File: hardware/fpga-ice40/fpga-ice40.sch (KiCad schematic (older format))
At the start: 85 parts, among them J1 MicroSD_Molex_1040310811, J2 ProgHeader_iCE40, J3 ProgHeader_Flash_QSPI, J4 Conn_02x20_Odd_Even, U1 iCE40HX4K-TQ144, U2 IS42S16320F-6TL, U3 W25Q32JVSS, U4 W25Q32JVSS, U5 S25FL256SAGMFI01, U6 S25FL256SAGMFI01, U7 FT245RL

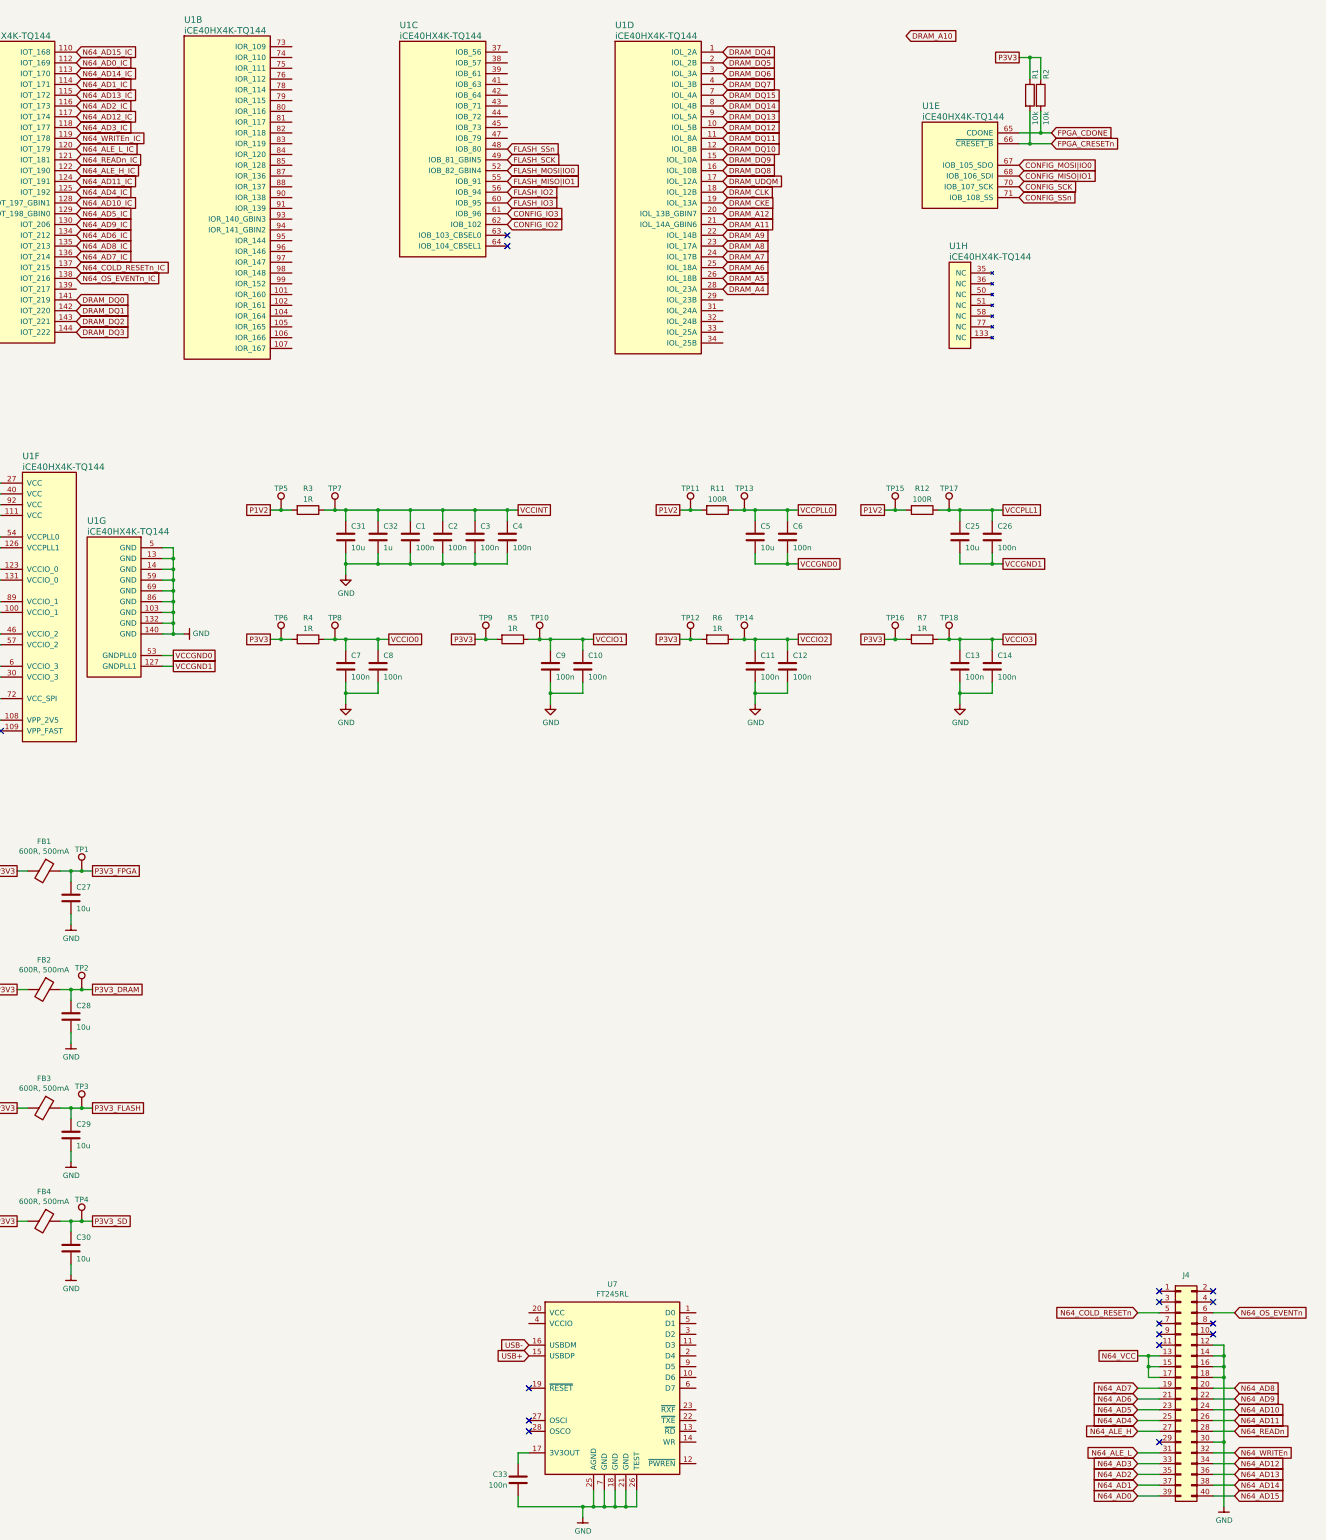
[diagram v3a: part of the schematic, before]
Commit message: Routing fpga to memory
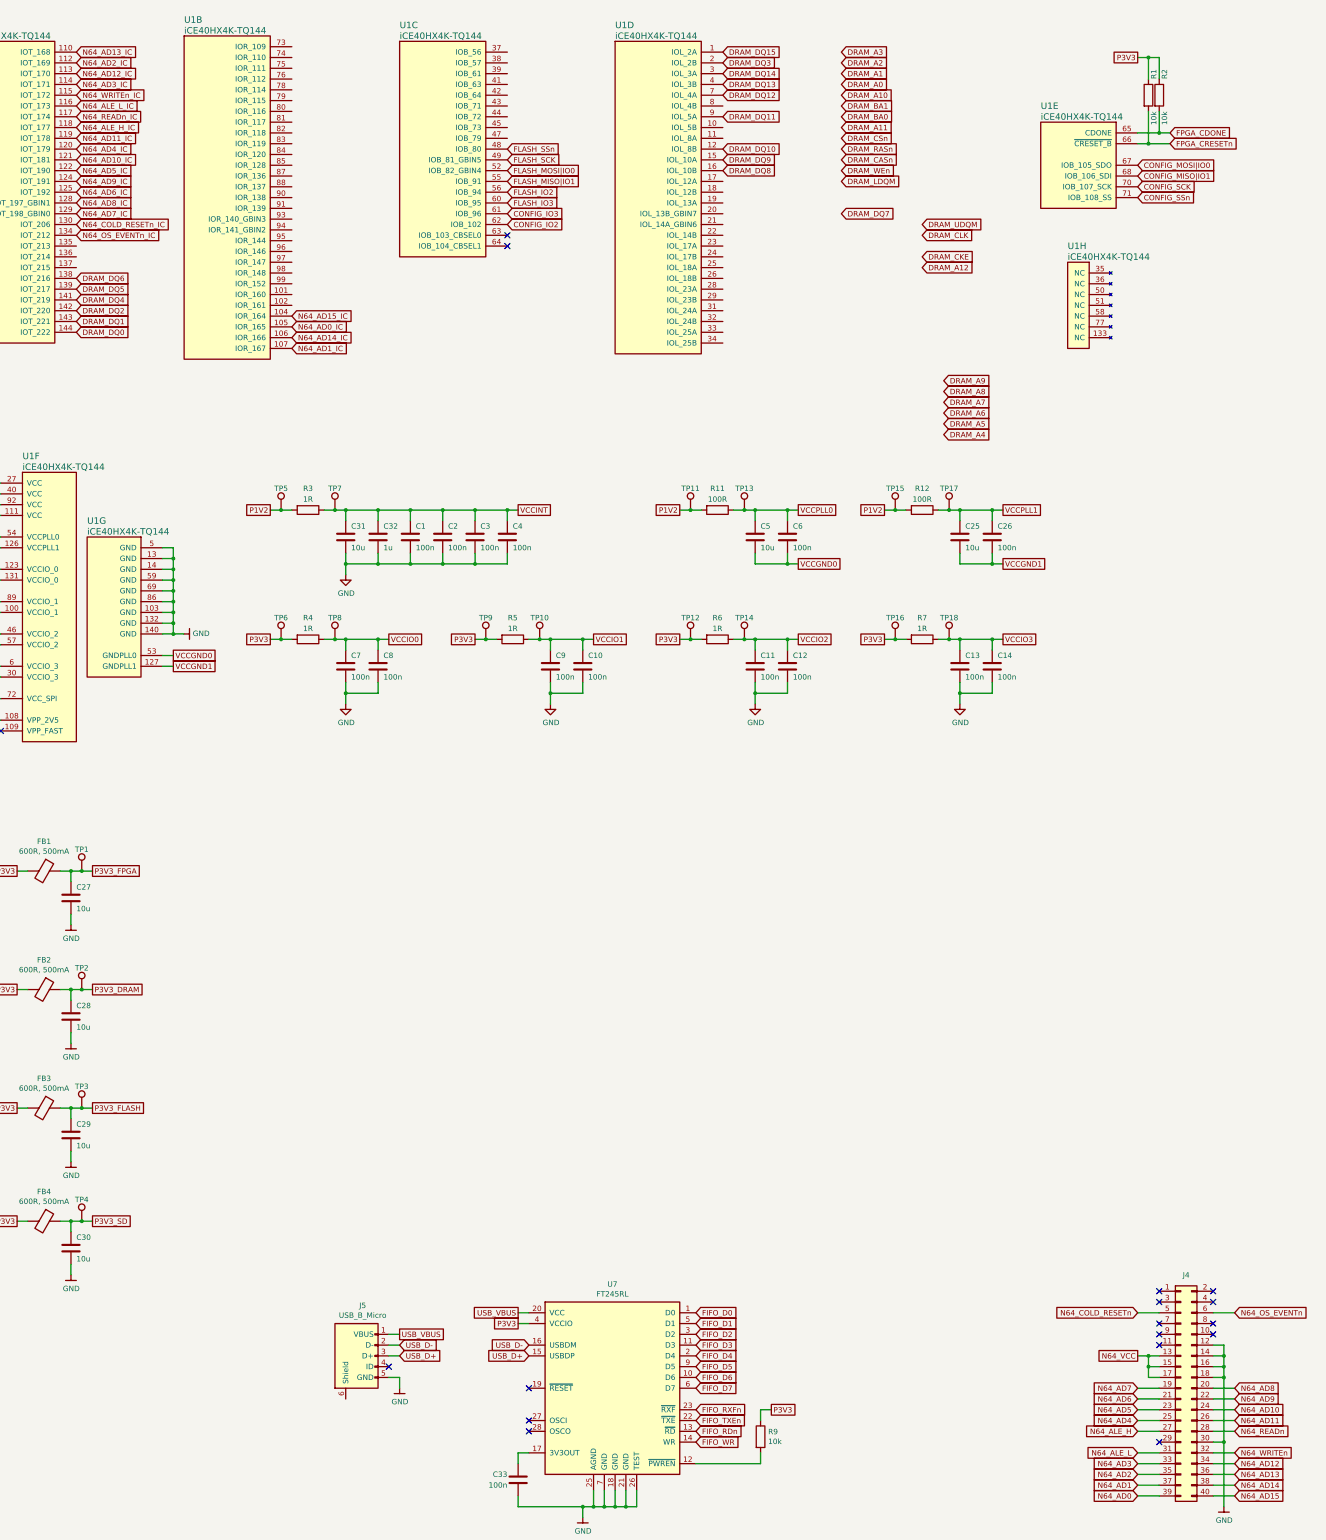
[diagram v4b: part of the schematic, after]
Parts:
- added J5: USB_B_Micro, Connector_USB:USB_Micro-B_Wuerth_629105150521, symbol ng_conn:USB_B_Micro
- added R9: 10k, Resistor_SMD:R_0603_1608Metric, symbol Device:R
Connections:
- net DRAM_A11: no longer U1.21 (IOL_14A_GBIN6)
- net DRAM_A12: no longer U1.20 (IOL_13B_GBIN7)
- net DRAM_A4: no longer U1.28 (IOL_23A)
- net DRAM_A5: no longer U1.26 (IOL_18B)
- net DRAM_A6: no longer U1.25 (IOL_18A)
- net DRAM_A7: no longer U1.24 (IOL_17B)
- net DRAM_A8: no longer U1.23 (IOL_17A)
- net DRAM_A9: no longer U1.22 (IOL_14B)
- net DRAM_CKE: no longer U1.19 (IOL_13A)
- net DRAM_CLK: no longer U1.18 (IOL_12B)
- net DRAM_DQ0: now also U1.144 (IOT_222); no longer U1.141 (IOT_219)
- net DRAM_DQ1: now also U1.143 (IOT_221); no longer U1.142 (IOT_220)
- net DRAM_DQ11: now also U1.9 (IOL_5A); no longer U1.11 (IOL_8A)
- net DRAM_DQ12: now also U1.7 (IOL_4A); no longer U1.10 (IOL_5B)
- net DRAM_DQ13: now also U1.4 (IOL_3B); no longer U1.9 (IOL_5A)
- net DRAM_DQ14: now also U1.3 (IOL_3A); no longer U1.8 (IOL_4B)
- net DRAM_DQ15: now also U1.1 (IOL_2A); no longer U1.7 (IOL_4A)
- net DRAM_DQ2: now also U1.142 (IOT_220); no longer U1.143 (IOT_221)
- net DRAM_DQ3: now also U1.2 (IOL_2B); no longer U1.144 (IOT_222)
- net DRAM_DQ4: now also U1.141 (IOT_219); no longer U1.1 (IOL_2A)
- net DRAM_DQ5: now also U1.139 (IOT_217); no longer U1.2 (IOL_2B)
- net DRAM_DQ6: now also U1.138 (IOT_216); no longer U1.3 (IOL_3A)
- net DRAM_DQ7: no longer U1.4 (IOL_3B)
- net DRAM_UDQM: no longer U1.17 (IOL_12A)
- net GND: now also J5.5 (GND)
- net N64_AD0_IC: now also U1.105 (IOR_165); no longer U1.112 (IOT_169)
- net N64_AD10_IC: now also U1.121 (IOT_181); no longer U1.128 (IOT_197_GBIN1)
- net N64_AD11_IC: now also U1.119 (IOT_178); no longer U1.124 (IOT_191)
- net N64_AD12_IC: now also U1.113 (IOT_170); no longer U1.117 (IOT_174)
- net N64_AD13_IC: now also U1.110 (IOT_168); no longer U1.115 (IOT_172)
- net N64_AD14_IC: now also U1.106 (IOR_166); no longer U1.113 (IOT_170)
- net N64_AD15_IC: now also U1.104 (IOR_164); no longer U1.110 (IOT_168)
- net N64_AD1_IC: now also U1.107 (IOR_167); no longer U1.114 (IOT_171)
- net N64_AD2_IC: now also U1.112 (IOT_169); no longer U1.116 (IOT_173)
- net N64_AD3_IC: now also U1.114 (IOT_171); no longer U1.118 (IOT_177)
- net N64_AD4_IC: now also U1.120 (IOT_179); no longer U1.125 (IOT_192)
- net N64_AD5_IC: now also U1.122 (IOT_190); no longer U1.129 (IOT_198_GBIN0)
- net N64_AD6_IC: now also U1.125 (IOT_192); no longer U1.134 (IOT_212)
- net N64_AD7_IC: now also U1.129 (IOT_198_GBIN0); no longer U1.136 (IOT_214)
- net N64_AD8_IC: now also U1.128 (IOT_197_GBIN1); no longer U1.135 (IOT_213)
- net N64_AD9_IC: now also U1.124 (IOT_191); no longer U1.130 (IOT_206)
- net N64_ALE_H_IC: now also U1.118 (IOT_177); no longer U1.122 (IOT_190)
- net N64_ALE_L_IC: now also U1.116 (IOT_173); no longer U1.120 (IOT_179)
- net N64_COLD_RESETn_IC: now also U1.130 (IOT_206); no longer U1.137 (IOT_215)
- net N64_OS_EVENTn_IC: now also U1.134 (IOT_212); no longer U1.138 (IOT_216)
- net N64_READn_IC: now also U1.117 (IOT_174); no longer U1.121 (IOT_181)
- net N64_WRITEn_IC: now also U1.115 (IOT_172); no longer U1.119 (IOT_178)
- net P3V3: now also U7.4 (VCCIO), R9.1
- net FIFO_D0: now reaches U7.1 (D0)
- net FIFO_D6: now reaches U7.10 (D6)
- net FIFO_D3: now reaches U7.11 (D3)
- net at U7.12 (~PWREN): now also R9.2
- net FIFO_RDn: now reaches U7.13 (~RD)
- net FIFO_WR: now reaches U7.14 (WR)
- net FIFO_D4: now reaches U7.2 (D4)
- net USB_VBUS: now reaches U7.20 (VCC)
- net USB_VBUS: now also J5.1 (VBUS)
- net FIFO_TXEn: now reaches U7.22 (~TXE)
- net FIFO_RXFn: now reaches U7.23 (~RXF)
- net FIFO_D2: now reaches U7.3 (D2)
- net FIFO_D1: now reaches U7.5 (D1)
- net FIFO_D7: now reaches U7.6 (D7)
- net FIFO_D5: now reaches U7.9 (D5)
- net USB+ renamed USB_D+
- net USB_D+: now also J5.3 (D+)
- net USB- renamed USB_D-
- net USB_D-: now also J5.2 (D-)
- no-connect marks 21 -> 22
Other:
- moved on the sheet: R1, R2, U1E, U1H

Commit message: Routing FPGA to SPI flash memory and USB interface
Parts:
- removed FB1, FB2, FB3, FB4: 600R, 500mA, symbol Device:Ferrite_Bead
- removed J2: ProgHeader_iCE40, Connector_PinHeader_2.54mm:PinHeader_1x08_P2.54mm_Vertical, symbol local_conn:ProgHeader_iCE40
- removed J3: ProgHeader_Flash_QSPI, Connector_PinHeader_2.54mm:PinHeader_1x08_P2.54mm_Vertical, symbol local_conn:ProgHeader_Flash_QSPI
- removed R5, R6, R7: 1R, Resistor_SMD:R_0603_1608Metric, symbol Device:R
- removed TP1, TP10, TP11, TP12, TP13, TP14, TP15, TP16, TP17, TP18, TP2, TP3, TP4, TP5, TP6, TP7, TP8, TP9: TestPoint, symbol Connector:TestPoint
- added C34, C35, C36, C37, C38: 10u, Capacitor_SMD:C_0805_2012Metric, symbol Device:C
- added D1: D_Schottky, symbol Device:D_Schottky
- added J6, J7: Conn_02x05_Odd_Even, ng_conn:Samtec_FTSH-105-XX-X-DV, symbol Connector_Generic:Conn_02x05_Odd_Even
- added U8, U9: AZ1117-1.2, Package_TO_SOT_SMD:SOT-223-3_TabPin2, symbol Regulator_Linear:AZ1117-1.2
- C28, C29: value 10u -> 100n
- J5: footprint Connector_USB:USB_Micro-B_Wuerth_629105150521 -> Connector_USB:USB_Micro-B_Molex_47346-0001
- R3: value 1R -> 6k8
- R4: value 1R -> 10k
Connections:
- net P3V3_DRAM is gone; now on net P3V3: C15.1, C16.1, C17.1, C18.1, C19.1, C20.1, C21.1, C28.1, U2.1 (VDD), U2.14 (VDD), U2.27 (VDD), U2.3 (VDDQ), U2.43 (VDDQ), U2.49 (VDDQ), U2.9 (VDDQ)
- net P3V3_FPGA is gone; now on net P3V3: C27.1
- net P3V3_SD is gone; now on net P3V3: C24.1, C30.1, J1.4 (Pin_4), R8.1, RN3.5 (R4.2), RN3.6 (R3.2), RN3.7 (R2.2), RN3.8 (R1.2)
- net VCCIO1 is gone; now on net P3V3: C10.1, C9.1, U1.100 (VCCIO_1), U1.89 (VCCIO_1)
- net VCCIO2 is gone; now on net P3V3: C11.1, C12.1, U1.46 (VCCIO_2), U1.57 (VCCIO_2)
- net VCCIO3 is gone; now on net P3V3: C13.1, C14.1, U1.30 (VCCIO_3), U1.6 (VCCIO_3)
- net VCCSPI is gone; now on net P3V3: U1.72 (VCC_SPI)
- net CONFIG_IO2: now also RN1.2 (R2.1); no longer RN1.3 (R3.1)
- net CONFIG_MISO|IO1: now also J6.7 (Pin_7)
- net CONFIG_MOSI|IO0: now also J6.5 (Pin_5)
- net CONFIG_SCK: now also RN1.3 (R3.1), J6.1 (Pin_1); no longer RN1.2 (R2.1)
- net CONFIG_SSn: now also J6.10 (Pin_10)
- net DRAM_A0: now also U1.43 (IOB_71)
- net DRAM_A1: now also U1.42 (IOB_64)
- net DRAM_A10: now also U1.32 (IOL_24B)
- net DRAM_A11: now also U1.28 (IOL_23A)
- net DRAM_A12: now also U1.26 (IOL_18B)
- net DRAM_A2: now also U1.41 (IOB_63)
- net DRAM_A3: now also U1.39 (IOB_61)
- net DRAM_A4: now also U1.37 (IOB_56)
- net DRAM_A5: now also U1.38 (IOB_57)
- net DRAM_A6: now also U1.34 (IOL_25B)
- net DRAM_A7: now also U1.33 (IOL_25A)
- net DRAM_A8: now also U1.31 (IOL_24A)
- net DRAM_A9: now also U1.29 (IOL_23B)
- net DRAM_BA0: now also U1.21 (IOL_14A_GBIN6)
- net DRAM_BA1: now also U1.24 (IOL_17B)
- net DRAM_CASn: now also U1.18 (IOL_12B)
- net DRAM_CKE: now also U1.25 (IOL_18A)
- net DRAM_CLK: now also U1.23 (IOL_17A)
- net DRAM_CSn: now also U1.20 (IOL_13B_GBIN7)
- net DRAM_DQ10: now also U1.10 (IOL_5B); no longer U1.12 (IOL_8B)
- net DRAM_DQ12: now also U1.8 (IOL_4B); no longer U1.7 (IOL_4A)
- net DRAM_DQ3: now also U1.141 (IOT_219); no longer U1.2 (IOL_2B)
- net DRAM_DQ4: now also U1.2 (IOL_2B); no longer U1.141 (IOT_219)
- net DRAM_DQ6: now also U1.7 (IOL_4A); no longer U1.138 (IOT_216)
- net DRAM_DQ7: now also U1.12 (IOL_8B)
- net DRAM_DQ8: now also U1.17 (IOL_12A); no longer U1.16 (IOL_10B)
- net DRAM_DQ9: now also U1.11 (IOL_8A); no longer U1.15 (IOL_10A)
- net DRAM_LDQM: now also U1.15 (IOL_10A)
- net DRAM_RASn: now also U1.19 (IOL_13A)
- net DRAM_UDQM: now also U1.22 (IOL_14B)
- net DRAM_WEn: now also U1.16 (IOL_10B)
- net FIFO_D0: now also U1.107 (IOR_167)
- net FIFO_D1: now also U1.102 (IOR_161)
- net FIFO_D2: now also U1.105 (IOR_165)
- net FIFO_D3: now also U1.95 (IOR_144)
- net FIFO_D4: now also U1.106 (IOR_166)
- net FIFO_D5: now also U1.97 (IOR_147)
- net FIFO_D6: now also U1.96 (IOR_146)
- net FIFO_D7: now also U1.101 (IOR_160)
- net FIFO_RDn: now also U1.94 (IOR_141_GBIN2)
- net FIFO_RXFn: now also U1.104 (IOR_164)
- net FIFO_TXEn: now also U1.99 (IOR_152)
- net FIFO_WR: now also U1.93 (IOR_140_GBIN3)
- net FLASH_IO2: now also RN2.2 (R2.1), U1.49 (IOB_81_GBIN5), J7.9 (Pin_9); no longer RN2.3 (R3.1), U1.56 (IOB_94)
- net FLASH_IO3: now also J7.3 (Pin_3)
- net FLASH_MISO|IO1: now also U1.48 (IOB_80), J7.7 (Pin_7); no longer U1.55 (IOB_91)
- net FLASH_MOSI|IO0: now also J7.5 (Pin_5)
- net FLASH_SCK: now also RN2.3 (R3.1), U1.56 (IOB_94), J7.1 (Pin_1); no longer RN2.2 (R2.1), U1.49 (IOB_81_GBIN5)
- net FLASH_SSn: now also U1.55 (IOB_91), J7.10 (Pin_10); no longer U1.48 (IOB_80)
- net FPGA_CDONE: now also J6.8 (Pin_8)
- net FPGA_CRESETn: now also J6.9 (Pin_9)
- net GND: now also R4.2, C34.2, C35.2, C36.2, C37.2, C38.2, J6.2 (Pin_2), J6.4 (Pin_4), J7.2 (Pin_2), J7.4 (Pin_4), U8.1 (GND), U9.1 (GND)
- net N64_AD0_IC: now also U1.112 (IOT_169); no longer U1.105 (IOR_165)
- net N64_AD10_IC: now also U1.128 (IOT_197_GBIN1); no longer U1.121 (IOT_181)
- net N64_AD11_IC: now also U1.124 (IOT_191); no longer U1.119 (IOT_178)
- net N64_AD12_IC: now also U1.117 (IOT_174); no longer U1.113 (IOT_170)
- net N64_AD13_IC: now also U1.115 (IOT_172); no longer U1.110 (IOT_168)
- net N64_AD14_IC: now also U1.110 (IOT_168); no longer U1.106 (IOR_166)
- net N64_AD15_IC: now also U1.113 (IOT_170); no longer U1.104 (IOR_164)
- net N64_AD1_IC: now also U1.114 (IOT_171); no longer U1.107 (IOR_167)
- net N64_AD2_IC: now also U1.116 (IOT_173); no longer U1.112 (IOT_169)
- net N64_AD3_IC: now also U1.118 (IOT_177); no longer U1.114 (IOT_171)
- net N64_AD4_IC: now also U1.125 (IOT_192); no longer U1.120 (IOT_179)
- net N64_AD5_IC: now also U1.129 (IOT_198_GBIN0); no longer U1.122 (IOT_190)
- net N64_AD6_IC: now also U1.134 (IOT_212); no longer U1.125 (IOT_192)
- net N64_AD7_IC: now also U1.136 (IOT_214); no longer U1.129 (IOT_198_GBIN0)
- net N64_AD8_IC: now also U1.135 (IOT_213); no longer U1.128 (IOT_197_GBIN1)
- net N64_AD9_IC: now also U1.130 (IOT_206); no longer U1.124 (IOT_191)
- net N64_ALE_H_IC: now also U1.122 (IOT_190); no longer U1.118 (IOT_177)
- net N64_ALE_L_IC: now also U1.120 (IOT_179); no longer U1.116 (IOT_173)
- net N64_COLD_RESETn_IC: now also U1.137 (IOT_215); no longer U1.130 (IOT_206)
- net N64_OS_EVENTn_IC: now also U1.138 (IOT_216); no longer U1.134 (IOT_212)
- net N64_READn_IC: now also U1.121 (IOT_181); no longer U1.117 (IOT_174)
- net N64_WRITEn_IC: now also U1.119 (IOT_178); no longer U1.115 (IOT_172)
- net P1V2: now also C1.1, C2.1, C3.1, C31.1, C32.1, C4.1, U1.111 (VCC), U1.27 (VCC), U1.40 (VCC), U1.92 (VCC), C38.1, U9.2 (VO); no longer R3.2
- net P3V3: now also C22.1, C23.1, C7.1, C8.1, RN1.5 (R4.2), RN1.6 (R3.2), RN1.7 (R2.2), RN1.8 (R1.2), RN2.5 (R4.2), RN2.6 (R3.2), RN2.7 (R2.2), RN2.8 (R1.2), U1.123 (VCCIO_0), U1.131 (VCCIO_0), U3.8 (VCC), U4.8 (VCC), U5.14 ((VIO)), U5.2 (VCC), U5.3 ((~RESET~)), U6.14 ((VIO)), U6.2 (VCC), U6.3 ((~RESET~)), C37.1, D1.2 (A), J6.6 (Pin_6), J7.6 (Pin_6), U9.3 (VI); no longer R4.2, U7.4 (VCCIO)
- net USB_VBUS: now also R3.1, C34.1, U8.3 (VI)
- net VCC2V5: now also C29.1, D1.1 (K)
- net USB_DETn: now reaches U1.98 (IOR_148)
- net USB_DETn: now also R3.2, R4.1, U7.19 (~RESET)
- net USB_PWRENn: now reaches R9.2, U7.12 (~PWREN)
- net USB_VIO: now reaches C33.1, U7.17 (3V3OUT)
- net USB_VIO: now also U7.4 (VCCIO)
- net N64_VCC renamed N64_3V3
- net N64_3V3: now also C36.1
- removed net P3V3_FLASH: C22.1, C23.1, C29.1, RN1.5 (R4.2), RN1.6 (R3.2), RN1.7 (R2.2), RN1.8 (R1.2), RN2.5 (R4.2), RN2.6 (R3.2), RN2.7 (R2.2), RN2.8 (R1.2), U3.8 (VCC), U4.8 (VCC), U5.14 ((VIO)), U5.2 (VCC), U5.3 ((~RESET~)), U6.14 ((VIO)), U6.2 (VCC), U6.3 ((~RESET~))
- removed net VCCINT: C1.1, C2.1, C3.1, C31.1, C32.1, C4.1, R3.1, U1.111 (VCC), U1.27 (VCC), U1.40 (VCC), U1.92 (VCC)
- removed net VCCIO0: C7.1, C8.1, R4.1, U1.123 (VCCIO_0), U1.131 (VCCIO_0)
- new net USB_3V3: C35.1, U8.2 (VO)
- no-connect marks 22 -> 23
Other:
- moved on the sheet: C1, C10, C11, C12, C13, C14, C2, C25, C26, C3, C30, C31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
